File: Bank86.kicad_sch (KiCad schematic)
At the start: 1 part, among them U1 XCKU5P-FFVB676

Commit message: finishing schematic
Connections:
- net IO_L11N_AD1N_86_N: now reaches U1.A10 (IO_L11N_AD1N_86_N)
- net IO_L10N_AD2N_86_N: now reaches U1.A9 (IO_L10N_AD2N_86_N)
- net IO_L11P_AD1P_86_P: now reaches U1.B10 (IO_L11P_AD1P_86_P)
- net IO_L12N_AD0N_86_N: now reaches U1.B11 (IO_L12N_AD0N_86_N)
- net IO_L10P_AD2P_86_P: now reaches U1.B9 (IO_L10P_AD2P_86_P)
- net IO_L12P_AD0P_86_P: now reaches U1.C11 (IO_L12P_AD0P_86_P)
- net IO_L9N_AD3N_86_N: now reaches U1.C9 (IO_L9N_AD3N_86_N)
- net IO_L8N_HDGC_AD4N_86_N: now reaches U1.D10 (IO_L8N_HDGC_AD4N_86_N)
- net IO_L8P_HDGC_AD4P_86_P: now reaches U1.D11 (IO_L8P_HDGC_AD4P_86_P)
- net IO_L9P_AD3P_86_P: now reaches U1.D9 (IO_L9P_AD3P_86_P)
- net IO_L7N_HDGC_AD5N_86_N: now reaches U1.E10 (IO_L7N_HDGC_AD5N_86_N)
- net IO_L7P_HDGC_AD5P_86_P: now reaches U1.E11 (IO_L7P_HDGC_AD5P_86_P)
- net IO_L6P_HDGC_AD6P_86_P: now reaches U1.F10 (IO_L6P_HDGC_AD6P_86_P)
- net IO_L6N_HDGC_AD6N_86_N: now reaches U1.F9 (IO_L6N_HDGC_AD6N_86_N)
- net IO_L5P_HDGC_AD7P_86_P: now reaches U1.G10 (IO_L5P_HDGC_AD7P_86_P)
- net IO_L4N_AD8N_86_N: now reaches U1.G11 (IO_L4N_AD8N_86_N)
- net IO_L5N_HDGC_AD7N_86_N: now reaches U1.G9 (IO_L5N_HDGC_AD7N_86_N)
- net IO_L4P_AD8P_86_P: now reaches U1.H11 (IO_L4P_AD8P_86_P)
- net IO_L3N_AD9N_86_N: now reaches U1.H9 (IO_L3N_AD9N_86_N)
- net IO_L2N_AD10N_86_N: now reaches U1.J10 (IO_L2N_AD10N_86_N)
- net IO_L2P_AD10P_86_P: now reaches U1.J11 (IO_L2P_AD10P_86_P)
- net IO_L3P_AD9P_86_P: now reaches U1.J9 (IO_L3P_AD9P_86_P)
- net IO_L1P_AD11P_86_P: now reaches U1.K10 (IO_L1P_AD11P_86_P)
- net IO_L1N_AD11N_86_N: now reaches U1.K9 (IO_L1N_AD11N_86_N)
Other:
- moved on the sheet: U1H

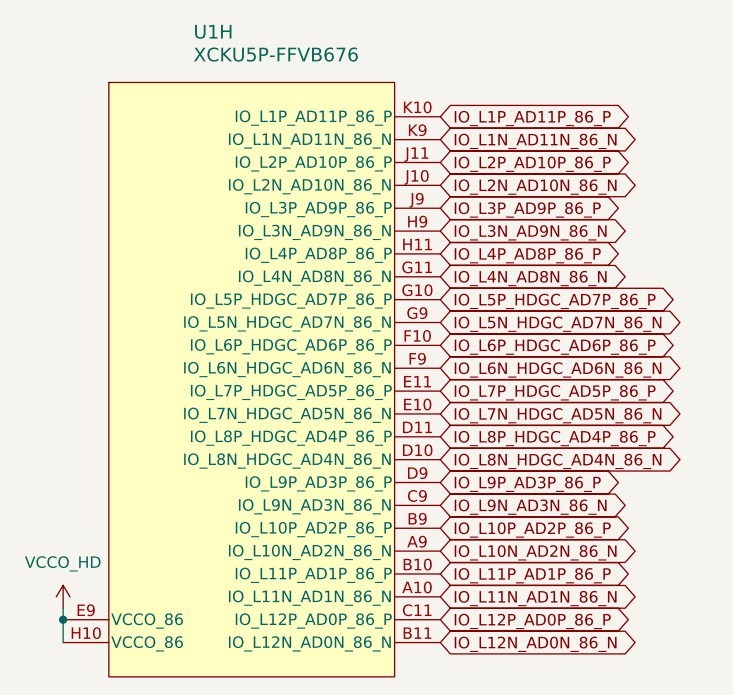
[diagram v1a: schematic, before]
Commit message: change net name to of IO diff pairs, add a scripts for name modification
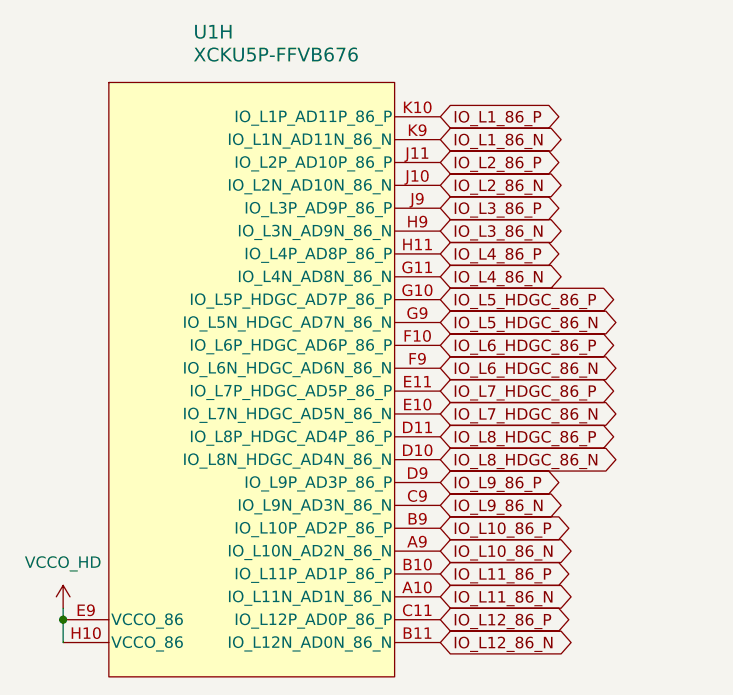
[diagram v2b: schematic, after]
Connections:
- net IO_L10N_AD2N_86_N renamed IO_L10_86_N
- net IO_L10P_AD2P_86_P renamed IO_L10_86_P
- net IO_L11N_AD1N_86_N renamed IO_L11_86_N
- net IO_L11P_AD1P_86_P renamed IO_L11_86_P
- net IO_L12N_AD0N_86_N renamed IO_L12_86_N
- net IO_L12P_AD0P_86_P renamed IO_L12_86_P
- net IO_L1N_AD11N_86_N renamed IO_L1_86_N
- net IO_L1P_AD11P_86_P renamed IO_L1_86_P
- net IO_L2N_AD10N_86_N renamed IO_L2_86_N
- net IO_L2P_AD10P_86_P renamed IO_L2_86_P
- net IO_L3N_AD9N_86_N renamed IO_L3_86_N
- net IO_L3P_AD9P_86_P renamed IO_L3_86_P
- net IO_L4N_AD8N_86_N renamed IO_L4_86_N
- net IO_L4P_AD8P_86_P renamed IO_L4_86_P
- net IO_L5N_HDGC_AD7N_86_N renamed IO_L5_HDGC_86_N
- net IO_L5P_HDGC_AD7P_86_P renamed IO_L5_HDGC_86_P
- net IO_L6N_HDGC_AD6N_86_N renamed IO_L6_HDGC_86_N
- net IO_L6P_HDGC_AD6P_86_P renamed IO_L6_HDGC_86_P
- net IO_L7N_HDGC_AD5N_86_N renamed IO_L7_HDGC_86_N
- net IO_L7P_HDGC_AD5P_86_P renamed IO_L7_HDGC_86_P
- net IO_L8N_HDGC_AD4N_86_N renamed IO_L8_HDGC_86_N
- net IO_L8P_HDGC_AD4P_86_P renamed IO_L8_HDGC_86_P
- net IO_L9N_AD3N_86_N renamed IO_L9_86_N
- net IO_L9P_AD3P_86_P renamed IO_L9_86_P
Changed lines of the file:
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@@
 		)
 	)
-	(global_label "IO_L3P_AD9P_86_P"
+	(global_label "IO_L3_86_P"
 		(shape bidirectional)
 		(at 99.06 66.04 0)
@@
 		)
 	)
-	(global_label "IO_L9P_AD3P_86_P"
+	(global_label "IO_L9_86_P"
 		(shape bidirectional)
 		(at 99.06 96.52 0)
@@
 		)
 	)
-	(global_label "IO_L4N_AD8N_86_N"
+	(global_label "IO_L4_86_N"
 		(shape bidirectional)
 		(at 99.06 73.66 0)
@@
 		)
 	)
-	(global_label "IO_L3N_AD9N_86_N"
+	(global_label "IO_L3_86_N"
 		(shape bidirectional)
 		(at 99.06 68.58 0)
@@
 		)
 	)
-	(global_label "IO_L1N_AD11N_86_N"
+	(global_label "IO_L1_86_N"
 		(shape bidirectional)
 		(at 99.06 58.42 0)
@@
 		)
 	)
-	(global_label "IO_L2N_AD10N_86_N"
+	(global_label "IO_L2_86_N"
 		(shape bidirectional)
 		(at 99.06 63.5 0)
@@
 		)
 	)
-	(global_label "IO_L6N_HDGC_AD6N_86_N"
+	(global_label "IO_L6_HDGC_86_N"
 		(shape bidirectional)
 		(at 99.06 83.82 0)
@@
 		)
 	)
-	(global_label "IO_L7P_HDGC_AD5P_86_P"
+	(global_label "IO_L7_HDGC_86_P"
 		(shape bidirectional)
 		(at 99.06 86.36 0)
@@
 		)
 	)
-	(global_label "IO_L12N_AD0N_86_N"
+	(global_label "IO_L12_86_N"
 		(shape bidirectional)
 		(at 99.06 114.3 0)
@@
 		)
 	)
-	(global_label "IO_L9N_AD3N_86_N"
+	(global_label "IO_L9_86_N"
 		(shape bidirectional)
 		(at 99.06 99.06 0)
@@
 		)
 	)
-	(global_label "IO_L10P_AD2P_86_P"
+	(global_label "IO_L10_86_P"
 		(shape bidirectional)
 		(at 99.06 101.6 0)
@@
 		)
 	)
-	(global_label "IO_L5N_HDGC_AD7N_86_N"
+	(global_label "IO_L5_HDGC_86_N"
 		(shape bidirectional)
 		(at 99.06 78.74 0)
@@
 		)
 	)
-	(global_label "IO_L5P_HDGC_AD7P_86_P"
+	(global_label "IO_L5_HDGC_86_P"
 		(shape bidirectional)
 		(at 99.06 76.2 0)
@@
 		)
 	)
-	(global_label "IO_L8P_HDGC_AD4P_86_P"
+	(global_label "IO_L8_HDGC_86_P"
 		(shape bidirectional)
 		(at 99.06 91.44 0)
@@
 		)
 	)
-	(global_label "IO_L11N_AD1N_86_N"
+	(global_label "IO_L11_86_N"
 		(shape bidirectional)
 		(at 99.06 109.22 0)
@@
 		)
 	)
-	(global_label "IO_L12P_AD0P_86_P"
+	(global_label "IO_L12_86_P"
 		(shape bidirectional)
 		(at 99.06 111.76 0)
@@
 		)
 	)
-	(global_label "IO_L11P_AD1P_86_P"
+	(global_label "IO_L11_86_P"
 		(shape bidirectional)
 		(at 99.06 106.68 0)
@@
 		)
 	)
-	(global_label "IO_L10N_AD2N_86_N"
+	(global_label "IO_L10_86_N"
 		(shape bidirectional)
 		(at 99.06 104.14 0)
@@
 		)
 	)
-	(global_label "IO_L7N_HDGC_AD5N_86_N"
+	(global_label "IO_L7_HDGC_86_N"
 		(shape bidirectional)
 		(at 99.06 88.9 0)
@@
 		)
 	)
-	(global_label "IO_L4P_AD8P_86_P"
+	(global_label "IO_L4_86_P"
 		(shape bidirectional)
 		(at 99.06 71.12 0)
@@
 		)
 	)
-	(global_label "IO_L1P_AD11P_86_P"
+	(global_label "IO_L1_86_P"
 		(shape bidirectional)
 		(at 99.06 55.88 0)
@@
 		)
 	)
-	(global_label "IO_L2P_AD10P_86_P"
+	(global_label "IO_L2_86_P"
 		(shape bidirectional)
 		(at 99.06 60.96 0)
@@
 		)
 	)
-	(global_label "IO_L8N_HDGC_AD4N_86_N"
+	(global_label "IO_L8_HDGC_86_N"
 		(shape bidirectional)
 		(at 99.06 93.98 0)
@@
 		)
 	)
-	(global_label "IO_L6P_HDGC_AD6P_86_P"
+	(global_label "IO_L6_HDGC_86_P"
 		(shape bidirectional)
 		(at 99.06 81.28 0)
